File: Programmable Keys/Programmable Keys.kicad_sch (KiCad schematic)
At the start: 22 parts, among them J1 Conn_01x05_Female, J2 Conn_01x05_Male

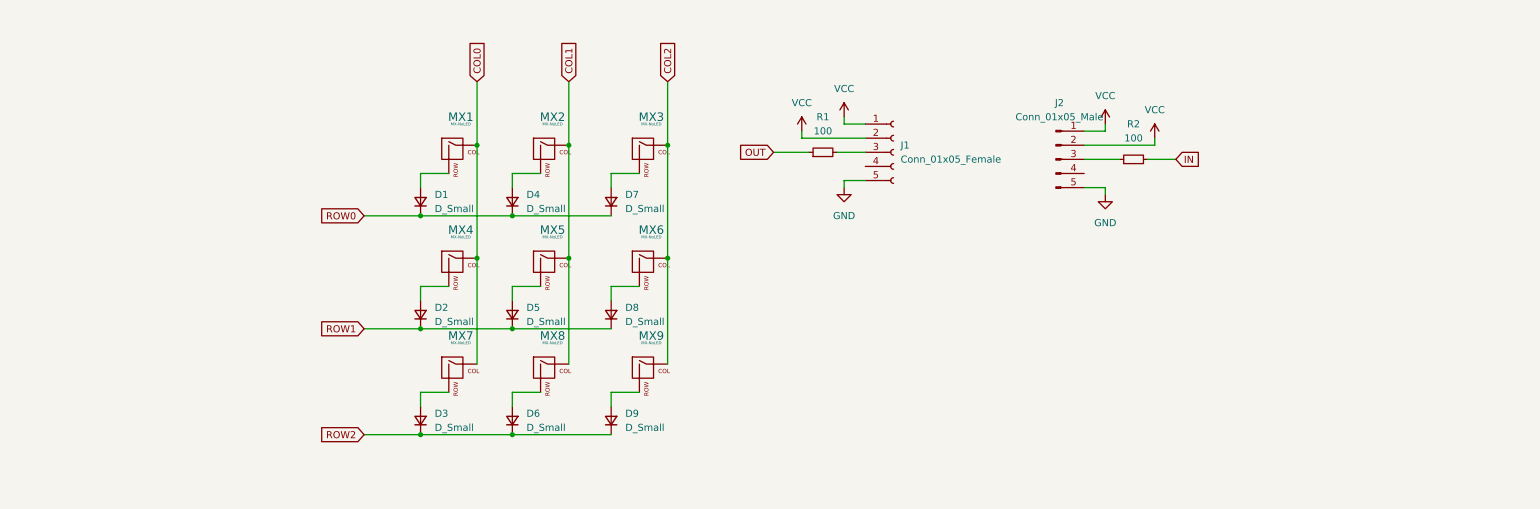
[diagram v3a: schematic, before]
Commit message: Updated connectors / footprint
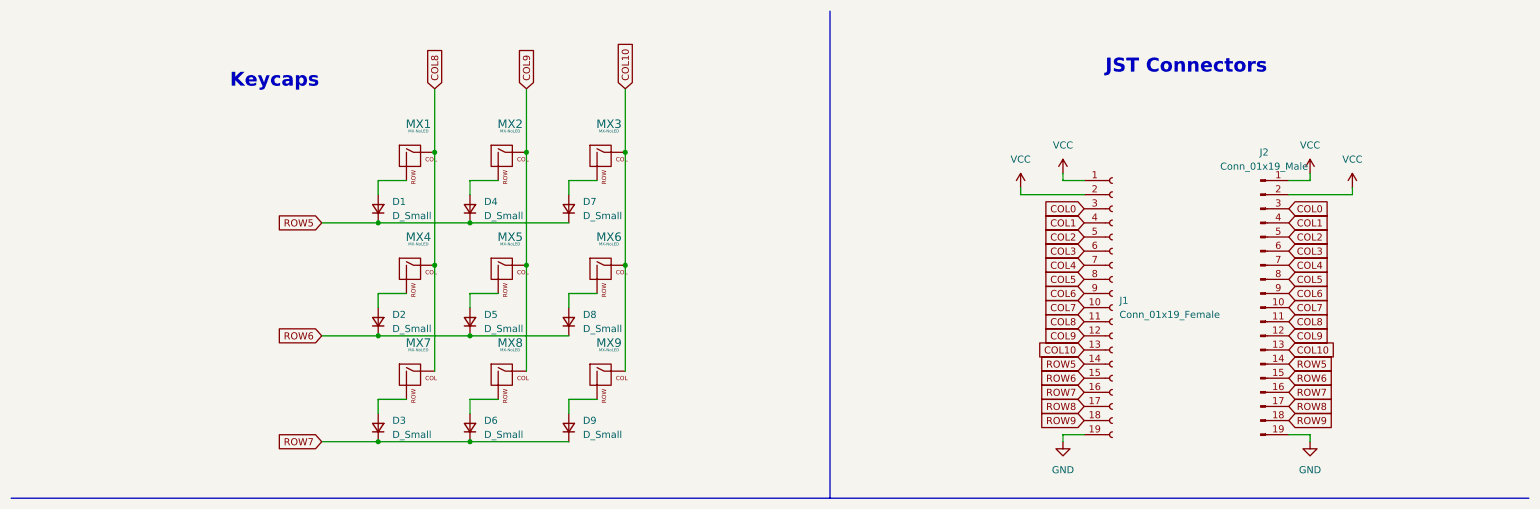
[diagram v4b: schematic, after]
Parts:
- removed J1: Conn_01x05_Female, Connector_JST:JST_PH_B5B-PH-K_1x05_P2.00mm_Vertical, symbol Connector:Conn_01x05_Female
- removed J2: Conn_01x05_Male, Connector_JST:JST_PH_B5B-PH-K_1x05_P2.00mm_Vertical, symbol Connector:Conn_01x05_Male
- removed R1, R2: 100, Resistor_SMD:R_0805_2012Metric, symbol Device:R_Small
- added J1: Conn_01x19_Female, Connector_JST:JST_SH_SM20B-SRSS-TB_1x20-1MP_P1.00mm_Horizontal, symbol Connector:Conn_01x19_Female
- added J2: Conn_01x19_Male, Connector_JST:JST_SH_SM20B-SRSS-TB_1x20-1MP_P1.00mm_Horizontal, symbol Connector:Conn_01x19_Male
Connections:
- net COL0: now also J1.3 (Pin_3), J2.3 (Pin_3); no longer MX1.1 (COL), MX4.1 (COL), MX7.1 (COL)
- net COL1: now also J1.4 (Pin_4), J2.4 (Pin_4); no longer MX2.1 (COL), MX5.1 (COL), MX8.1 (COL)
- net COL2: now also J1.5 (Pin_5), J2.5 (Pin_5); no longer MX3.1 (COL), MX6.1 (COL), MX9.1 (COL)
- net GND: now also J1.19 (Pin_19), J2.19 (Pin_19)
- net VCC: now also J1.1 (Pin_1), J1.2 (Pin_2), J2.1 (Pin_1), J2.2 (Pin_2)
- net ROW0 renamed ROW5
- net ROW5: now also J1.14 (Pin_14), J2.14 (Pin_14)
- net ROW1 renamed ROW6
- net ROW6: now also J1.15 (Pin_15), J2.15 (Pin_15)
- net ROW2 renamed ROW7
- net ROW7: now also J1.16 (Pin_16), J2.16 (Pin_16)
- new net COL10: J1.13 (Pin_13), J2.13 (Pin_13), MX3.1 (COL), MX6.1 (COL), MX9.1 (COL)
- new net COL3: J1.6 (Pin_6), J2.6 (Pin_6)
- new net COL4: J1.7 (Pin_7), J2.7 (Pin_7)
- new net COL5: J1.8 (Pin_8), J2.8 (Pin_8)
- new net COL6: J1.9 (Pin_9), J2.9 (Pin_9)
- new net COL7: J1.10 (Pin_10), J2.10 (Pin_10)
- new net COL8: J1.11 (Pin_11), J2.11 (Pin_11), MX1.1 (COL), MX4.1 (COL), MX7.1 (COL)
- new net COL9: J1.12 (Pin_12), J2.12 (Pin_12), MX2.1 (COL), MX5.1 (COL), MX8.1 (COL)
- new net ROW8: J1.17 (Pin_17), J2.17 (Pin_17)
- new net ROW9: J1.18 (Pin_18), J2.18 (Pin_18)
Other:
- note added: "JST Connectors"
- note added: "Keycaps"
- moved on the sheet: D1, D2, D3, D4, D5, D6, D7, D8, D9, MX1, MX2, MX3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

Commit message: Started wiring
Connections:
- net VCC: no longer J1.1 (Pin_1), J2.1 (Pin_1)
- new net +5V: J1.1 (Pin_1), J2.1 (Pin_1)
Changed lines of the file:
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@@
     (pin "2")
+  )
+  (symbol (lib_id "power:+5V") (at 201.93 40.64 0) (unit 1)
+    (in_bom yes) (on_board yes) (fields_autoplaced)
+    (property "Reference" "#PWR0106" (id 0) (at 201.93 44.45 0)
+      (effects (font (size 1.27 1.27)) hide)
+    )
+    (property "Value" "+5V" (id 1) (at 201.93 35.56 0))
+    (property "Footprint" "" (id 2) (at 201.93 40.64 0)
+      (effects (font (size 1.27 1.27)) hide)
+    )
+    (property "Datasheet" "" (id 3) (at 201.93 40.64 0)
+      (effects (font (size 1.27 1.27)) hide)
+    )
+    (pin "1")
   )
   (symbol (lib_id "MX_Alps_Hybrid:MX-NoLED") (at 85.09 77.47 0) (unit 1)
@@
     (pin "2")
   )
-  (symbol (lib_id "power:VCC") (at 246.38 40.64 0) (mirror y) (unit 1)
-    (in_bom yes) (on_board yes) (fields_autoplaced)
-    (property "Reference" "#PWR0106" (id 0) (at 246.38 44.45 0)
-      (effects (font (size 1.27 1.27)) hide)
-    )
-    (property "Value" "VCC" (id 1) (at 246.38 35.56 0))
-    (property "Footprint" "" (id 2) (at 246.38 40.64 0)
-      (effects (font (size 1.27 1.27)) hide)
-    )
-    (property "Datasheet" "" (id 3) (at 246.38 40.64 0)
-      (effects (font (size 1.27 1.27)) hide)
-    )
-    (pin "1")
-  )
   (symbol (lib_id "Device:D_Small") (at 113.03 86.36 90) (unit 1)
     (in_bom yes) (on_board yes) (fields_autoplaced)
@@
     (pin "1")
     (pin "2")
-  )
-  (symbol (lib_id "power:VCC") (at 201.93 40.64 0) (unit 1)
-    (in_bom yes) (on_board yes) (fields_autoplaced)
-    (property "Reference" "#PWR0101" (id 0) (at 201.93 44.45 0)
-      (effects (font (size 1.27 1.27)) hide)
-    )
-    (property "Value" "VCC" (id 1) (at 201.93 35.56 0))
-    (property "Footprint" "" (id 2) (at 201.93 40.64 0)
-      (effects (font (size 1.27 1.27)) hide)
-    )
-    (property "Datasheet" "" (id 3) (at 201.93 40.64 0)
-      (effects (font (size 1.27 1.27)) hide)
-    )
-    (pin "1")
   )
   (symbol (lib_id "Device:D_Small") (at 113.03 46.99 90) (unit 1)
@@
     (pin "2")
   )
+  (symbol (lib_id "power:+5V") (at 246.38 40.64 0) (unit 1)
+    (in_bom yes) (on_board yes) (fields_autoplaced)
+    (property "Reference" "#PWR0101" (id 0) (at 246.38 44.45 0)
+      (effects (font (size 1.27 1.27)) hide)
+    )
+    (property "Value" "+5V" (id 1) (at 246.38 35.56 0))
+    (property "Footprint" "" (id 2) (at 246.38 40.64 0)
+      (effects (font (size 1.27 1.27)) hide)
+    )
+    (property "Datasheet" "" (id 3) (at 246.38 40.64 0)
+      (effects (font (size 1.27 1.27)) hide)
+    )
+    (pin "1")
+  )
   (symbol (lib_id "MX_Alps_Hybrid:MX-NoLED") (at 85.09 58.42 0) (unit 1)
     (in_bom yes) (on_board yes) (fields_autoplaced)
@@
   )
   (symbol_instances
-    (path "/6d1cfc32-67e5-4ae6-882b-693efde8f764"
-      (reference "#PWR0101") (unit 1) (value "VCC") (footprint "")
+    (path "/8cc8e8db-8803-4bf3-a39a-ec110a84ce5e"
+      (reference "#PWR0101") (unit 1) (value "+5V") (footprint "")
     )
     (path "/2b0ffd5a-6584-4ee3-9d52-d4853391bc15"
@@
       (reference "#PWR0105") (unit 1) (value "VCC") (footprint "")
     )
-    (path "/5ef9e26c-3fc0-460e-b66f-448efdc00e90"
-      (reference "#PWR0106") (unit 1) (value "VCC") (footprint "")
+    (path "/3ec3b264-b9e2-4360-8885-2cf54bd78fb2"
+      (reference "#PWR0106") (unit 1) (value "+5V") (footprint "")
     )
     (path "/deaeb746-0d3d-4bb0-a186-8c685d641314"

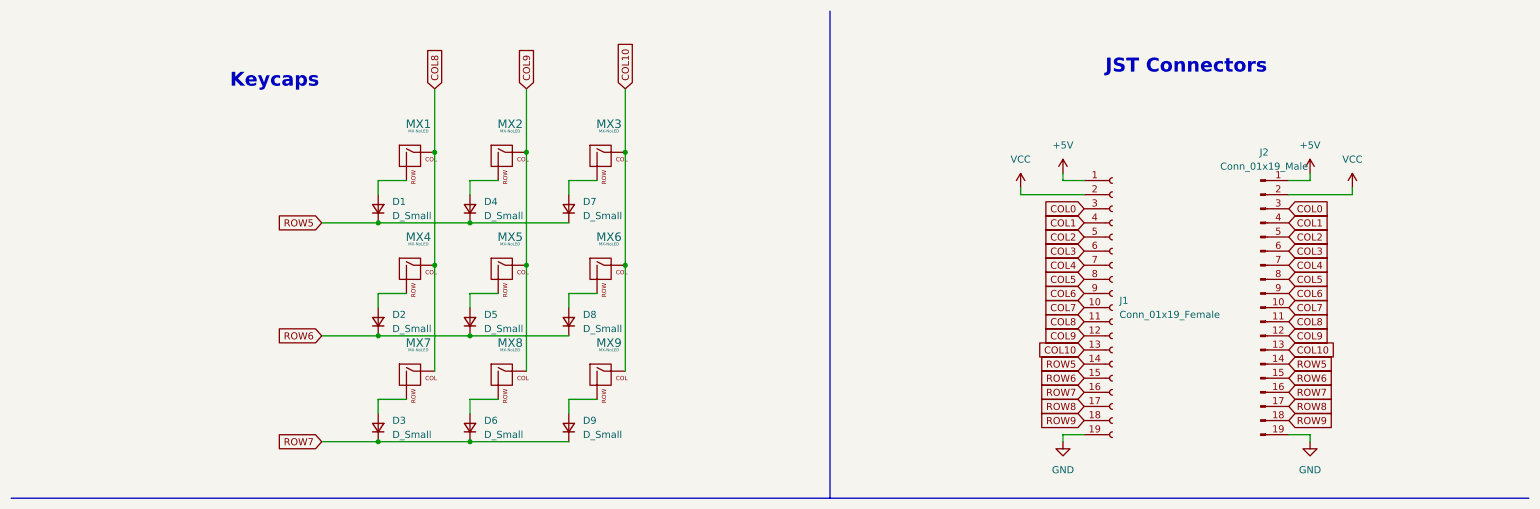
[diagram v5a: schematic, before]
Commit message: Updated connectors + added mounting holes
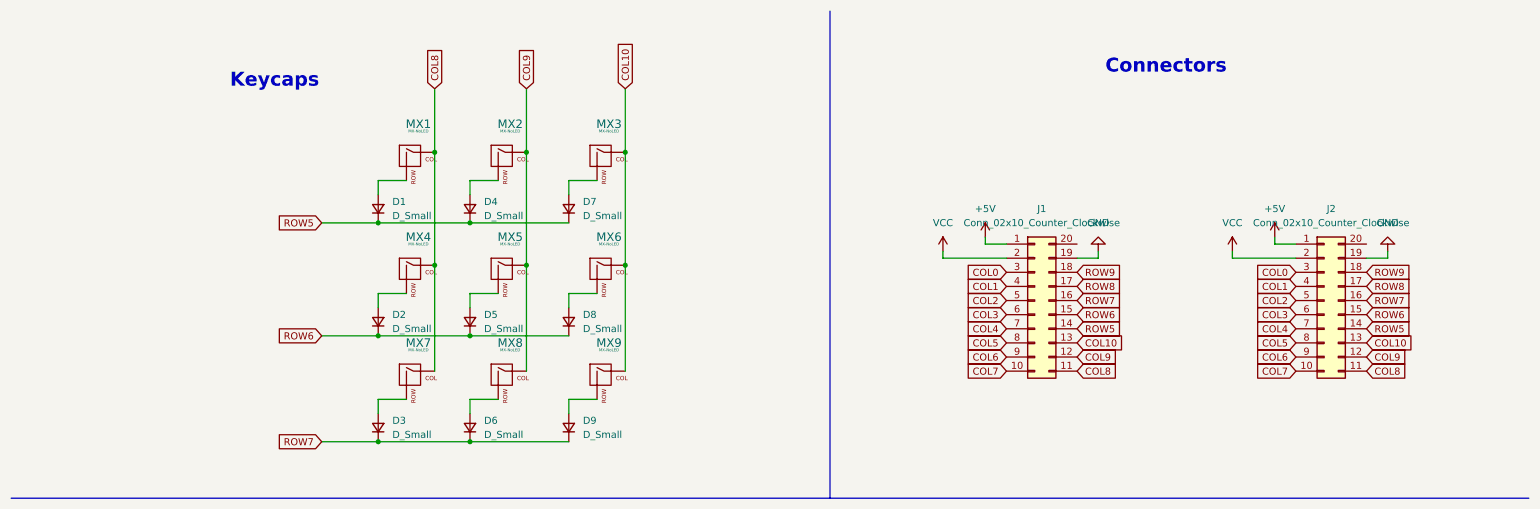
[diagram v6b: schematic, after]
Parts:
- removed J1: Conn_01x19_Female, Connector_JST:JST_SH_SM20B-SRSS-TB_1x20-1MP_P1.00mm_Horizontal, symbol Connector:Conn_01x19_Female
- removed J2: Conn_01x19_Male, Connector_JST:JST_SH_SM20B-SRSS-TB_1x20-1MP_P1.00mm_Horizontal, symbol Connector:Conn_01x19_Male
- added J1: Conn_02x10_Counter_Clockwise, Connector_PinSocket_2.54mm:PinSocket_2x10_P2.54mm_Horizontal, symbol Connector_Generic:Conn_02x10_Counter_Clockwise
- added J2: Conn_02x10_Counter_Clockwise, Connector_PinHeader_2.54mm:PinHeader_2x10_P2.54mm_Horizontal, symbol Connector_Generic:Conn_02x10_Counter_Clockwise
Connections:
- net +5V: now also J1.1 (Pin_1), J2.1 (Pin_1)
- net COL0: now also J1.3 (Pin_3), J2.3 (Pin_3)
- net COL1: now also J1.4 (Pin_4), J2.4 (Pin_4)
- net COL10: now also J1.13 (Pin_13), J2.13 (Pin_13)
- net COL2: now also J1.5 (Pin_5), J2.5 (Pin_5)
- net COL3: now also J1.6 (Pin_6), J2.6 (Pin_6)
- net COL4: now also J1.7 (Pin_7), J2.7 (Pin_7)
- net COL5: now also J1.8 (Pin_8), J2.8 (Pin_8)
- net COL6: now also J1.9 (Pin_9), J2.9 (Pin_9)
- net COL7: now also J1.10 (Pin_10), J2.10 (Pin_10)
- net COL8: now also J1.11 (Pin_11), J2.11 (Pin_11)
- net COL9: now also J1.12 (Pin_12), J2.12 (Pin_12)
- net GND: now also J1.19 (Pin_19), J2.19 (Pin_19)
- net ROW5: now also J1.14 (Pin_14), J2.14 (Pin_14)
- net ROW6: now also J1.15 (Pin_15), J2.15 (Pin_15)
- net ROW7: now also J1.16 (Pin_16), J2.16 (Pin_16)
- net ROW8: now also J1.17 (Pin_17), J2.17 (Pin_17)
- net ROW9: now also J1.18 (Pin_18), J2.18 (Pin_18)
- net VCC: now also J1.2 (Pin_2), J2.2 (Pin_2)
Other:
- note added: "Connectors"
- note removed: "JST Connectors"
